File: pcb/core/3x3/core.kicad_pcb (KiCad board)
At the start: 2 copper layers, 79.3 x 78.9 mm, 29 parts, among them J1 Conn_01x11, J2 Conn_01x11, J3 Conn_01x04, SW1 SW_Push_45deg, SW10 RotaryEncoder_Switch, SW11 RotaryEncoder_Switch, SW2 SW_Push_45deg, SW3 SW_Push_45deg, SW4 SW_Push_45deg, SW5 SW_Push_45deg, SW6 SW_Push_45deg, SW7 SW_Push_45deg, SW8 SW_Push_45deg, SW9 SW_Push_45deg, U1 Helios

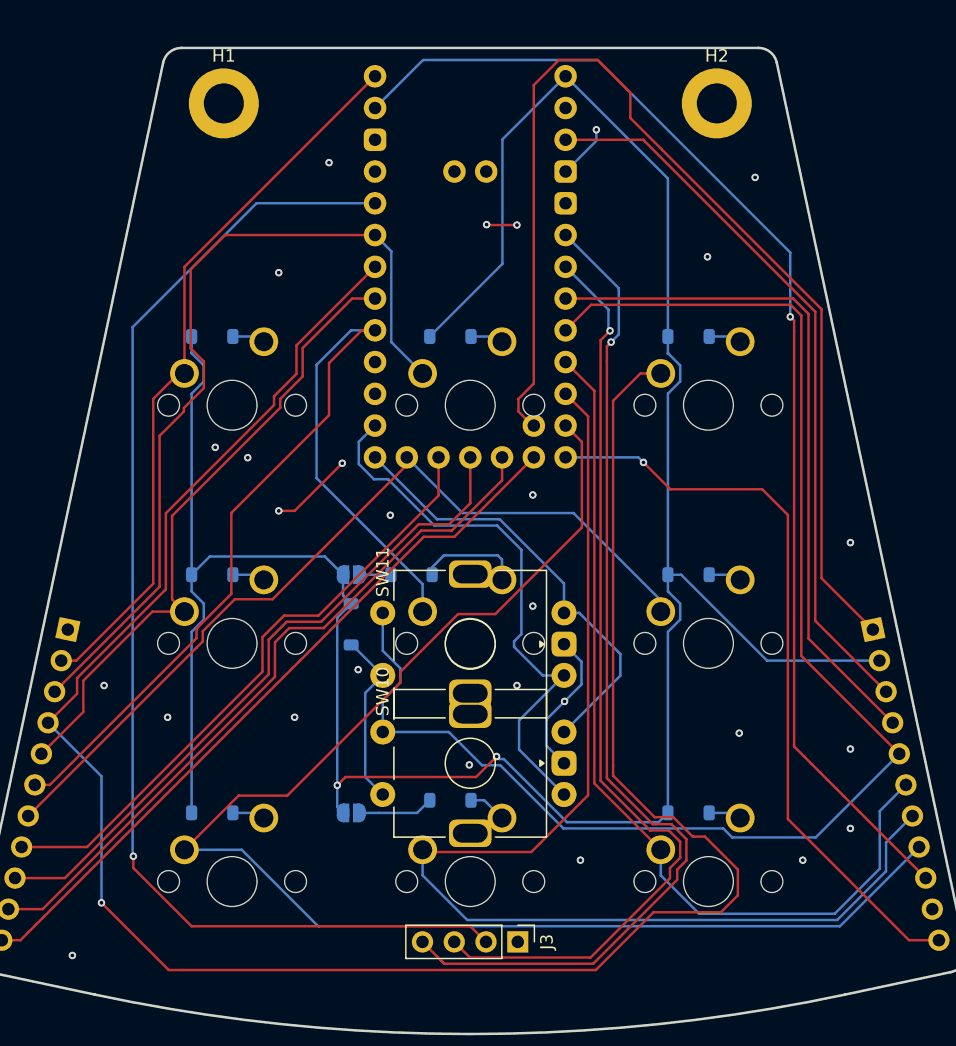
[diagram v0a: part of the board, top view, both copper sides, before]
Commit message: added two additional encoders
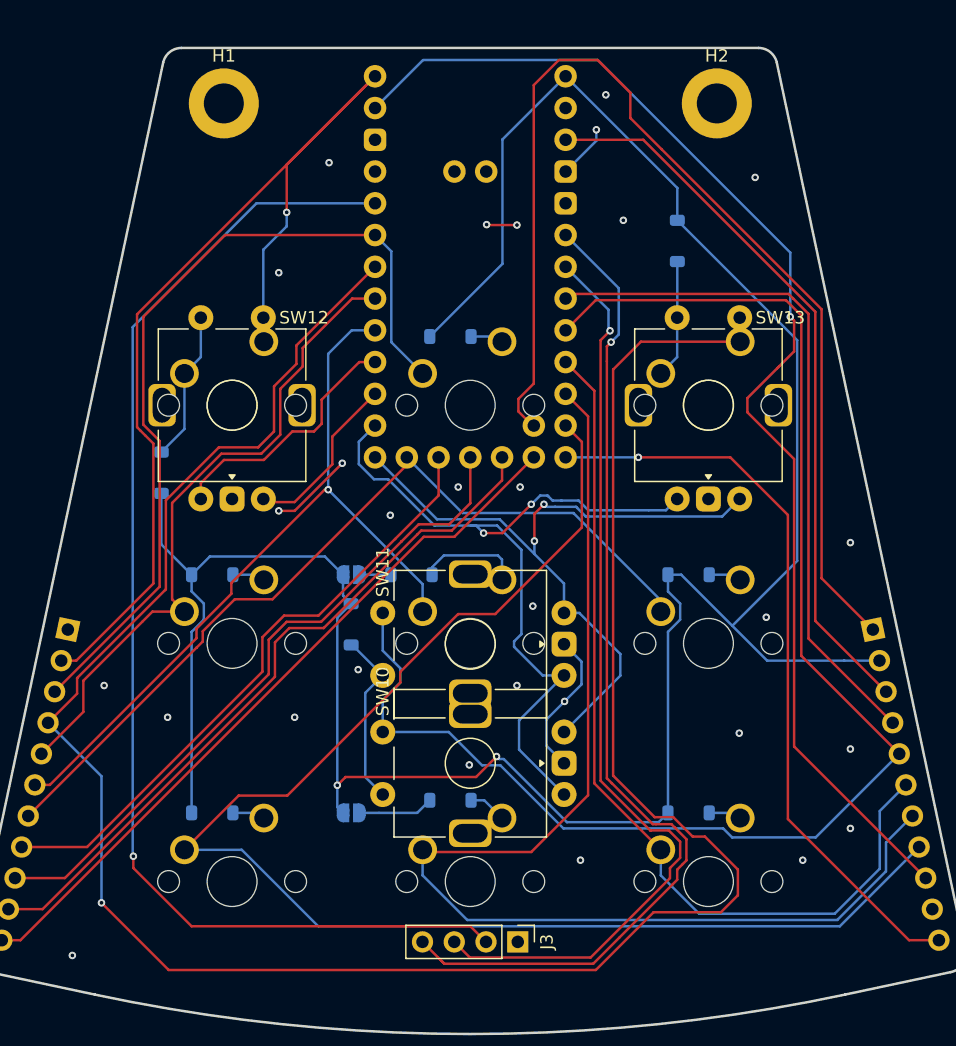
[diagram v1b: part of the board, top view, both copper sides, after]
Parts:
- added SW12: RotaryEncoder_Switch, PCM_marbastlib-various:ROT_Alps_EC11E-Switch, F.Cu at (179.1, 163.0)
- added SW13: RotaryEncoder_Switch, PCM_marbastlib-various:ROT_Alps_EC11E-Switch, F.Cu at (217.2, 163.0)
- moved D1 11.6 mm to (173.5, 168.4), turned to 90 degrees
- moved D3 7.70 mm to (214.8, 149.9), turned to -90 degrees
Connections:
- SW1 pad 1: col0 -> Net-(D1-A)
- SW1 pad 2: Net-(D1-A) -> col0
- SW3 pad 1: col2 -> Net-(D3-A)
- SW3 pad 2: Net-(D3-A) -> col2
- U1 pad 21: unconnected-(U1-P22-Pad21) -> enc2
- U1 pad 22: unconnected-(U1-P20-Pad22) -> enc3
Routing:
- net col0: track 58.1 -> 82.5 mm, vias 0 -> 1
- net enc1: track 35.6 -> 56.5 mm, vias 0 -> 2
- net enc2: track 0.00 -> 20.3 mm
- net enc0: track 44.9 -> 64.6 mm, vias 0 -> 2
- net col4: track 78.0 -> 62.5 mm, vias 0 -> 1
- net enc3: track 0.00 -> 14.5 mm
- net col2: track 168.9 -> 180.2 mm
- net Net-(D1-A): track 2.65 -> 12.5 mm
- net Net-(D3-A): track 2.65 -> 9.50 mm
- net raw: track 95.7 -> 99.0 mm
- net row5: track 211.9 -> 209.3 mm
- net col3: track 50.9 -> 52.7 mm
- net GND: vias 28 -> 29
